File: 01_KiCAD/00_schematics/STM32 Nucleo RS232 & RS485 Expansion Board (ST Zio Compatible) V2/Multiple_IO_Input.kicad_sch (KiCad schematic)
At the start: 0 parts

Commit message: Added components and change device
Added dual Schmidt trigger input SN74LVC2G14DBV for LED Rx and Tx control.
Changed sn74hcs245 for alternate part sn74lvc245a for larger footprint and better availability with LCSC.
Difference is sn74lvc245a has no Schmidt-trigger inputs but instead just normal inputs. Fot details see dataseet. Both devices use exact same pin number and configuration except sn74lvc245a has no thermal pad or exposed pad like the sn74hcs245 has.
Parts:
- added C26: 100nF, PCM_SparkFun-Capacitor:C_0603_1608Metric, symbol PCM_SparkFun-Capacitor:0.1uF_0603_25V_20%
- added D7: LED, IN-S63AT:LED_0603_WRE, symbol PCM_SparkFun-LED:LED
- added J6: HEADER 3POS 2.54mm, symbol Connector_Generic:Conn_01x03
- added Q2: BSS84, Package_TO_SOT_SMD:SOT-23, symbol Transistor_FET:BSS84
- added R23, R24, R37: 100K, PCM_fab:R_0603, symbol PCM_fab:R_0603
- added R32, R33, R36: 10K, PCM_fab:R_0603, symbol PCM_fab:R_0603
- added R34: 1K, PCM_fab:R_0603, symbol PCM_fab:R_0603
- added R35: 590R, PCM_fab:R_0603, symbol PCM_fab:R_0603
- added U3: SN74LVC245ADBR, SN74LVC245ADBR:SOP65P780X200-20N, symbol SN74LVC245ADBR:SN74HCS245RKSR
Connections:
- new net: J6.2 (Pin_2), R37.1, U3.19 (*OE)
- new net: Q2.1 (G), R34.1, R36.1
- new net: D7.2 (A), R35.2
- new net: R24.1, U3.9 (A8)
- new net: R32.2, U3.1 (DIR)
- new net: R23.1, U3.11 (B8)
- new net: J6.1 (Pin_1), R33.2
- new net 3V3_SYS: C26.1, R32.1, R33.1, U3.20 (VCC)
- new net DIR: U3.15 (B4)
- new net GND: C26.2, D7.1 (K), Q2.2 (S), R23.2, R24.2, R36.2, R37.2, U3.10 (GND)
- new net MCU_DIR: U3.5 (A4)
- new net MCU_MODE0: U3.6 (A5)
- new net MCU_MODE1: U3.7 (A6)
- new net MCU_MODE2: U3.8 (A7)
- new net MCU_OE: J6.3 (Pin_3), R35.1
- new net MCU_SLR: U3.2 (A1)
- new net MCU_TERM_RX: U3.4 (A3)
- new net MCU_TERM_TX: U3.3 (A2)
- new net MODE0: U3.14 (B5)
- new net MODE1: U3.13 (B6)
- new net MODE2: U3.12 (B7)
- new net SLR: U3.18 (B1)
- new net TERM_RX: U3.16 (B3)
- new net TERM_TX: U3.17 (B2)

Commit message: Finisching touches to schematics
Finalizing the schematics and double-check all connections throughout the different sheets.
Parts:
- renumbered Q2 to Q1, R34 to R20, R36 to R21, R33 to R22, R32 to R23, R23 to R25, R35 to R26, R37 to R27, U3 to U4
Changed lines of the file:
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@@
 		(dnp no)
 		(fields_autoplaced yes)
-		(property "Reference" "#PWR039"
+		(property "Reference" "#PWR040"
 			(at 144.78 121.92 0)
 			(effects
@@
 			(project "STM32 Nucleo RS232 & RS485 Expansion Board (ST Zio Compatible) V2"
 				(path "/080f83b7-8913-48e8-ab8e-79cb12295542/486090d1-223c-4361-8c2c-169c4ca9272f"
-					(reference "#PWR039")
+					(reference "#PWR040")
 					(unit 1)
 				)
@@
 		(dnp no)
 		(fields_autoplaced yes)
-		(property "Reference" "#PWR038"
+		(property "Reference" "#PWR042"
 			(at 220.98 121.92 0)
 			(effects
@@
 			(project "STM32 Nucleo RS232 & RS485 Expansion Board (ST Zio Compatible) V2"
 				(path "/080f83b7-8913-48e8-ab8e-79cb12295542/486090d1-223c-4361-8c2c-169c4ca9272f"
-					(reference "#PWR038")
+					(reference "#PWR042")
 					(unit 1)
 				)
@@
 		(dnp no)
 		(fields_autoplaced yes)
-		(property "Reference" "R37"
+		(property "Reference" "R27"
 			(at 134.62 105.4099 0)
 			(effects
@@
 			(project "STM32 Nucleo RS232 & RS485 Expansion Board (ST Zio Compatible) V2"
 				(path "/080f83b7-8913-48e8-ab8e-79cb12295542/486090d1-223c-4361-8c2c-169c4ca9272f"
-					(reference "R37")
+					(reference "R27")
 					(unit 1)
 				)
@@
 		(on_board yes)
 		(dnp no)
-		(property "Reference" "Q2"
+		(property "Reference" "Q1"
 			(at -38.1 72.3901 0)
 			(effects
@@
 			(project ""
 				(path "/080f83b7-8913-48e8-ab8e-79cb12295542/486090d1-223c-4361-8c2c-169c4ca9272f"
-					(reference "Q2")
+					(reference "Q1")
 					(unit 1)
 				)
@@
 		(on_board yes)
 		(dnp no)
-		(property "Reference" "R35"
+		(property "Reference" "R26"
 			(at 87.63 105.4099 0)
 			(effects
@@
 			(project "STM32 Nucleo RS232 & RS485 Expansion Board (ST Zio Compatible) V2"
 				(path "/080f83b7-8913-48e8-ab8e-79cb12295542/486090d1-223c-4361-8c2c-169c4ca9272f"
-					(reference "R35")
+					(reference "R26")
 					(unit 1)
 				)
@@
 		(dnp no)
 		(fields_autoplaced yes)
-		(property "Reference" "R32"
+		(property "Reference" "R23"
 			(at 106.68 81.2799 0)
 			(effects
@@
 			(project "STM32 Nucleo RS232 & RS485 Expansion Board (ST Zio Compatible) V2"
 				(path "/080f83b7-8913-48e8-ab8e-79cb12295542/486090d1-223c-4361-8c2c-169c4ca9272f"
-					(reference "R32")
+					(reference "R23")
 					(unit 1)
 				)
@@
 		(dnp no)
 		(fields_autoplaced yes)
-		(property "Reference" "U3"
+		(property "Reference" "U4"
 			(at 185.0233 63.5 0)
 			(effects
@@
 			(project ""
 				(path "/080f83b7-8913-48e8-ab8e-79cb12295542/486090d1-223c-4361-8c2c-169c4ca9272f"
-					(reference "U3")
+					(reference "U4")
 					(unit 1)
 				)
@@
 		(dnp no)
 		(fields_autoplaced yes)
-		(property "Reference" "#PWR040"
+		(property "Reference" "#PWR041"
 			(at 182.88 121.92 0)
 			(effects
@@
 			(project "STM32 Nucleo RS232 & RS485 Expansion Board (ST Zio Compatible) V2"
 				(path "/080f83b7-8913-48e8-ab8e-79cb12295542/486090d1-223c-4361-8c2c-169c4ca9272f"
-					(reference "#PWR040")
+					(reference "#PWR041")
 					(unit 1)
 				)
@@
 		(dnp no)
 		(fields_autoplaced yes)
-		(property "Reference" "#PWR042"
+		(property "Reference" "#PWR037"
 			(at 173.99 63.5 0)
 			(effects
@@
 			(project "STM32 Nucleo RS232 & RS485 Expansion Board (ST Zio Compatible) V2"
 				(path "/080f83b7-8913-48e8-ab8e-79cb12295542/486090d1-223c-4361-8c2c-169c4ca9272f"
-					(reference "#PWR042")
+					(reference "#PWR037")
 					(unit 1)
 				)
@@
 		(on_board yes)
 		(dnp no)
-		(property "Reference" "R23"
+		(property "Reference" "R25"
 			(at 209.55 101.6 90)
 			(effects
@@
 			(project "STM32 Nucleo RS232 & RS485 Expansion Board (ST Zio Compatible) V2"
 				(path "/080f83b7-8913-48e8-ab8e-79cb12295542/486090d1-223c-4361-8c2c-169c4ca9272f"
-					(reference "R23")
+					(reference "R25")
 					(unit 1)
 				)
@@
 		(dnp no)
 		(fields_autoplaced yes)
-		(property "Reference" "R36"
+		(property "Reference" "R21"
 			(at -21.59 77.4699 0)
 			(effects
@@
 			(project "STM32 Nucleo RS232 & RS485 Expansion Board (ST Zio Compatible) V2"
 				(path "/080f83b7-8913-48e8-ab8e-79cb12295542/486090d1-223c-4361-8c2c-169c4ca9272f"
-					(reference "R36")
+					(reference "R21")
 					(unit 1)
 				)
@@
 		(dnp no)
 		(fields_autoplaced yes)
-		(property "Reference" "#PWR044"
+		(property "Reference" "#PWR038"
 			(at -34.29 102.87 0)
 			(effects
@@
 			(project "STM32 Nucleo RS232 & RS485 Expansion Board (ST Zio Compatible) V2"
 				(path "/080f83b7-8913-48e8-ab8e-79cb12295542/486090d1-223c-4361-8c2c-169c4ca9272f"
-					(reference "#PWR044")
+					(reference "#PWR038")
 					(unit 1)
 				)
@@
 		(dnp no)
 		(fields_autoplaced yes)
-		(property "Reference" "R33"
+		(property "Reference" "R22"
 			(at 87.63 81.2799 0)
 			(effects
@@
 			(project "STM32 Nucleo RS232 & RS485 Expansion Board (ST Zio Compatible) V2"
 				(path "/080f83b7-8913-48e8-ab8e-79cb12295542/486090d1-223c-4361-8c2c-169c4ca9272f"
-					(reference "R33")
+					(reference "R22")
 					(unit 1)
 				)
@@
 		(dnp no)
 		(fields_autoplaced yes)
-		(property "Reference" "#PWR047"
+		(property "Reference" "#PWR039"
 			(at 132.08 121.92 0)
 			(effects
@@
 			(project "STM32 Nucleo RS232 & RS485 Expansion Board (ST Zio Compatible) V2"
 				(path "/080f83b7-8913-48e8-ab8e-79cb12295542/486090d1-223c-4361-8c2c-169c4ca9272f"
-					(reference "#PWR047")
+					(reference "#PWR039")
 					(unit 1)
 				)
@@
 		(on_board yes)
 		(dnp no)
-		(property "Reference" "R34"
+		(property "Reference" "R20"
 			(at -18.542 66.04 90)
 			(effects
@@
 			(project "STM32 Nucleo RS232 & RS485 Expansion Board (ST Zio Compatible) V2"
 				(path "/080f83b7-8913-48e8-ab8e-79cb12295542/486090d1-223c-4361-8c2c-169c4ca9272f"
-					(reference "R34")
+					(reference "R20")
 					(unit 1)
 				)

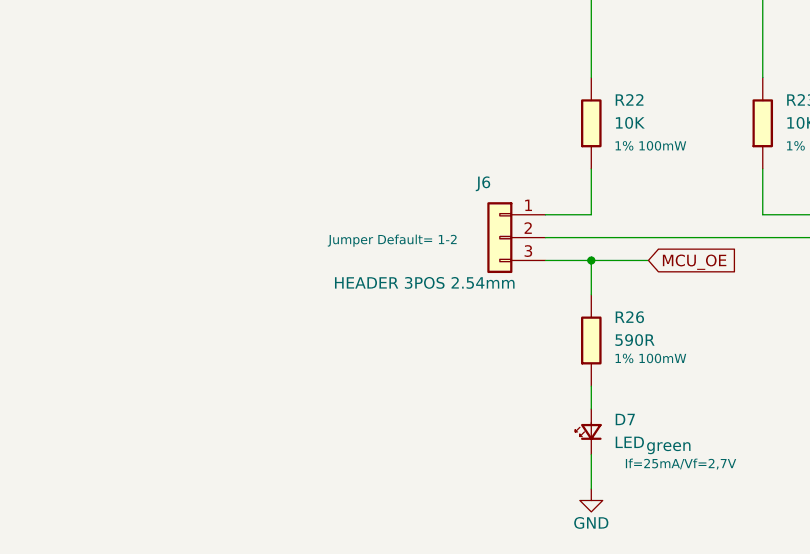
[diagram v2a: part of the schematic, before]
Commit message: Finishing up the schematic aand created the board outline
Made some finishing touches to the schematic, updated all the symbol footprints and started to create the board.
Added missing 3D models for Phoenix 4-p RS485 connector and RS232 connector, also for Inolux LED.
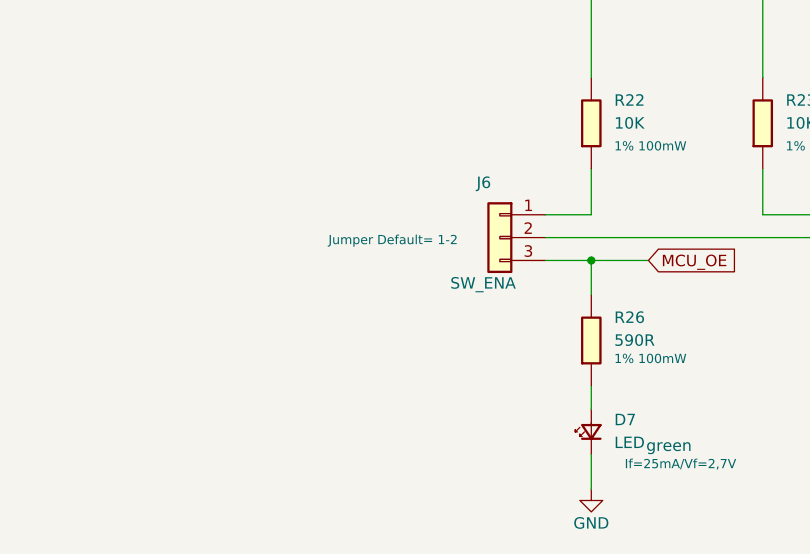
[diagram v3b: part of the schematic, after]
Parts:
- J6: value HEADER 3POS 2.54mm -> SW_ENA; footprint (none) -> HTSW-103-07-F-S:CON3_1X3_TU_TSW
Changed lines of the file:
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@@
 		(dnp no)
 		(fields_autoplaced yes)
-		(property "Reference" "#PWR040"
+		(property "Reference" "#PWR042"
 			(at 144.78 121.92 0)
 			(effects
@@
 			(project "STM32 Nucleo RS232 & RS485 Expansion Board (ST Zio Compatible) V2"
 				(path "/080f83b7-8913-48e8-ab8e-79cb12295542/486090d1-223c-4361-8c2c-169c4ca9272f"
-					(reference "#PWR040")
+					(reference "#PWR042")
 					(unit 1)
 				)
@@
 		(dnp no)
 		(fields_autoplaced yes)
-		(property "Reference" "#PWR043"
+		(property "Reference" "#PWR045"
 			(at 85.09 130.81 0)
 			(effects
@@
 			(project "STM32 Nucleo RS232 & RS485 Expansion Board (ST Zio Compatible) V2"
 				(path "/080f83b7-8913-48e8-ab8e-79cb12295542/486090d1-223c-4361-8c2c-169c4ca9272f"
-					(reference "#PWR043")
+					(reference "#PWR045")
 					(unit 1)
 				)
@@
 		(dnp no)
 		(fields_autoplaced yes)
-		(property "Reference" "#PWR042"
+		(property "Reference" "#PWR044"
 			(at 220.98 121.92 0)
 			(effects
@@
 			(project "STM32 Nucleo RS232 & RS485 Expansion Board (ST Zio Compatible) V2"
 				(path "/080f83b7-8913-48e8-ab8e-79cb12295542/486090d1-223c-4361-8c2c-169c4ca9272f"
-					(reference "#PWR042")
+					(reference "#PWR044")
 					(unit 1)
 				)
@@
 			)
 		)
-		(property "Value" "HEADER 3POS 2.54mm"
+		(property "Value" "SW_ENA"
 			(at 76.708 101.6 0)
 			(effects
@@
 			)
 		)
-		(property "Footprint" ""
+		(property "Footprint" "HTSW-103-07-F-S:CON3_1X3_TU_TSW"
 			(at 74.93 96.52 0)
 			(effects
@@
 			)
 		)
-		(property "Datasheet" "https://www.lcsc.com/datasheet/C6631883.pdf"
+		(property "Datasheet" "~"
 			(at 74.93 96.52 0)
 			(effects
@@
 			)
 		)
-		(property "Description" "Pin Header 3 Position 2.54mm Pitch Single Row Through Hole -55℃~+125℃"
+		(property "Description" "Generic connector, single row, 01x03, script generated (kicad-library-utils/schlib/autogen/connector/)"
 			(at 74.93 96.52 0)
 			(effects
@@
 		(dnp no)
 		(fields_autoplaced yes)
-		(property "Reference" "#PWR041"
+		(property "Reference" "#PWR043"
 			(at 182.88 121.92 0)
 			(effects
@@
 			(project "STM32 Nucleo RS232 & RS485 Expansion Board (ST Zio Compatible) V2"
 				(path "/080f83b7-8913-48e8-ab8e-79cb12295542/486090d1-223c-4361-8c2c-169c4ca9272f"
-					(reference "#PWR041")
+					(reference "#PWR043")
 					(unit 1)
 				)
@@
 		(dnp no)
 		(fields_autoplaced yes)
-		(property "Reference" "#PWR037"
+		(property "Reference" "#PWR039"
 			(at 173.99 63.5 0)
 			(effects
@@
 			(project "STM32 Nucleo RS232 & RS485 Expansion Board (ST Zio Compatible) V2"
 				(path "/080f83b7-8913-48e8-ab8e-79cb12295542/486090d1-223c-4361-8c2c-169c4ca9272f"
-					(reference "#PWR037")
+					(reference "#PWR039")
 					(unit 1)
 				)
@@
 		(dnp no)
 		(fields_autoplaced yes)
-		(property "Reference" "#PWR038"
+		(property "Reference" "#PWR040"
 			(at -34.29 102.87 0)
 			(effects
@@
 			(project "STM32 Nucleo RS232 & RS485 Expansion Board (ST Zio Compatible) V2"
 				(path "/080f83b7-8913-48e8-ab8e-79cb12295542/486090d1-223c-4361-8c2c-169c4ca9272f"
-					(reference "#PWR038")
+					(reference "#PWR040")
 					(unit 1)
 				)
@@
 		(dnp no)
 		(fields_autoplaced yes)
-		(property "Reference" "#PWR039"
+		(property "Reference" "#PWR041"
 			(at 132.08 121.92 0)
 			(effects
@@
 			(project "STM32 Nucleo RS232 & RS485 Expansion Board (ST Zio Compatible) V2"
 				(path "/080f83b7-8913-48e8-ab8e-79cb12295542/486090d1-223c-4361-8c2c-169c4ca9272f"
-					(reference "#PWR039")
+					(reference "#PWR041")
 					(unit 1)
 				)

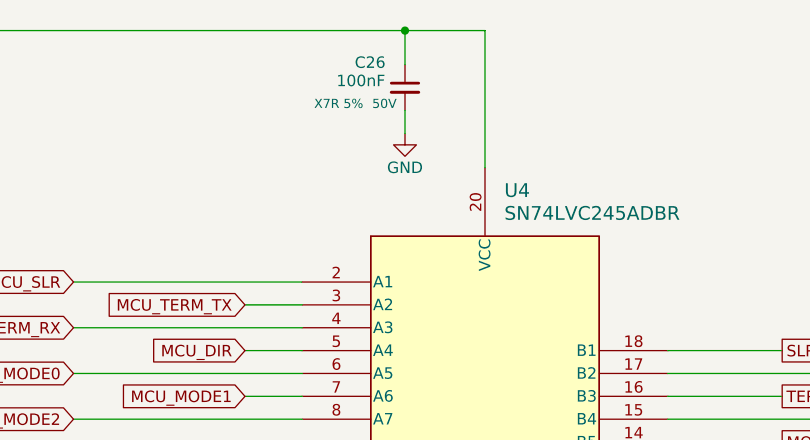
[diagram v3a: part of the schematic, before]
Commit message: Updated footprints and added components to PCB
Added some additional components to the board. Changed the footprint of the 3-pin Jumper so the bottom silkscreen text doesnlt overlap with the Dual Schmidt Trigger IC's SN74LVC2G14
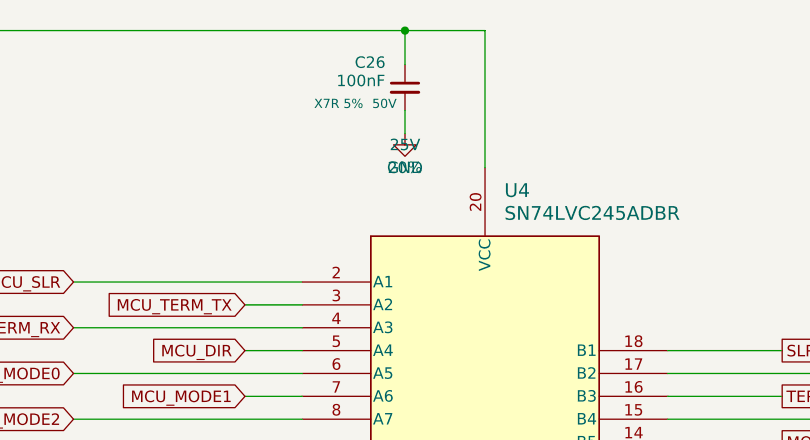
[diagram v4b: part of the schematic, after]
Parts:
- C26: PROD_ID (none) -> CAP-00810; Tolerance (none) -> 20%; Voltage (none) -> 25V
- J6: footprint HTSW-103-07-F-S:CON3_1X3_TU_TSW -> Samtec_Connector:Samtec HTSW-103-07-F-S
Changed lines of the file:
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@@
 			)
 		)
-		(property "Datasheet" "https://www.lcsc.com/datasheet/C14675.pdf"
+		(property "Datasheet" "~"
 			(at 132.08 107.95 0)
 			(effects
@@
 			)
 		)
-		(property "Description" "100mW 100kΩ 75V Thick Film Resistor ±100ppm/℃ ±1% 0603 Chip Resistor - Surface Mount RoHS"
+		(property "Description" "Resistor"
 			(at 132.08 107.95 0)
 			(effects
@@
 			)
 		)
-		(property "Datasheet" "https://www.lcsc.com/datasheet/C91183.pdf"
+		(property "Datasheet" "https://cdn.sparkfun.com/assets/8/a/4/a/5/Kemet_Capacitor_Datasheet.pdf"
 			(at 173.99 66.04 0)
 			(effects
@@
 			)
 		)
-		(property "Description" "100nF ±5% 50V Ceramic Capacitor X7R 0603"
+		(property "Description" "Unpolarized capacitor"
 			(at 173.99 71.12 0)
 			(effects
@@
 					(size 1.016 1.016)
 					(color 194 0 0 1)
+				)
+			)
+		)
+		(property "PROD_ID" "CAP-00810"
+			(at 173.99 68.58 0)
+			(effects
+				(font
+					(size 1.27 1.27)
+				)
+				(hide yes)
+			)
+		)
+		(property "Voltage" "25V"
+			(at 173.99 58.42 0)
+			(effects
+				(font
+					(size 1.27 1.27)
+				)
+			)
+		)
+		(property "Tolerance" "20%"
+			(at 173.99 60.96 0)
+			(effects
+				(font
+					(size 1.27 1.27)
 				)
 			)
@@
 			)
 		)
-		(property "Datasheet" "https://www.lcsc.com/datasheet/C22548.pdf"
+		(property "Datasheet" "~"
 			(at 85.09 107.95 0)
 			(effects
@@
 			)
 		)
-		(property "Description" "100mW 1kΩ 75V Thick Film Resistor ±100ppm/℃ ±1% 0603 Chip Resistor - Surface Mount RoHS"
+		(property "Description" "Resistor"
 			(at 85.09 107.95 0)
 			(effects
@@
 			)
 		)
-		(property "Datasheet" "https://www.lcsc.com/datasheet/C14675.pdf"
+		(property "Datasheet" "~"
 			(at 156.21 99.06 0)
 			(effects
@@
 			)
 		)
-		(property "Description" "100mW 100kΩ 75V Thick Film Resistor ±100ppm/℃ ±1% 0603 Chip Resistor - Surface Mount RoHS"
+		(property "Description" "Resistor"
 			(at 156.21 99.06 0)
 			(effects
@@
 			)
 		)
-		(property "Datasheet" "https://www.lcsc.com/datasheet/C98220.pdf"
+		(property "Datasheet" "~"
 			(at 104.14 83.82 0)
 			(effects
@@
 			)
 		)
-		(property "Description" "100mW 10kΩ 75V Thick Film Resistor ±100ppm/℃ ±1% 0603 Chip Resistor - Surface Mount RoHS"
+		(property "Description" "Resistor"
 			(at 104.14 83.82 0)
 			(effects
@@
 			)
 		)
-		(property "Footprint" "HTSW-103-07-F-S:CON3_1X3_TU_TSW"
+		(property "Footprint" "Samtec_Connector:Samtec HTSW-103-07-F-S"
 			(at 74.93 96.52 0)
 			(effects
@@
 			)
 		)
-		(property "Datasheet" "https://www.lcsc.com/datasheet/C14675.pdf"
+		(property "Datasheet" "~"
 			(at 209.55 99.06 0)
 			(effects
@@
 			)
 		)
-		(property "Description" "100mW 100kΩ 75V Thick Film Resistor ±100ppm/℃ ±1% 0603 Chip Resistor - Surface Mount RoHS"
+		(property "Description" "Resistor"
 			(at 209.55 99.06 0)
 			(effects
@@
 			)
 		)
-		(property "Datasheet" "https://www.lcsc.com/datasheet/C98220.pdf"
+		(property "Datasheet" "~"
 			(at -24.13 80.01 0)
 			(effects
@@
 			)
 		)
-		(property "Description" "100mW 10kΩ 75V Thick Film Resistor ±100ppm/℃ ±1% 0603 Chip Resistor - Surface Mount RoHS"
+		(property "Description" "Resistor"
 			(at -24.13 80.01 0)
 			(effects
@@
 			)
 		)
-		(property "Datasheet" "https://www.lcsc.com/datasheet/C5656662.pdf"
+		(property "Datasheet" "~"
 			(at 92.71 118.11 0)
 			(effects
@@
 			)
 		)
-		(property "Description" "Emerald Green 530nm LED Indication - Discrete 2.7V 0603"
+		(property "Description" "Light emitting diode"
 			(at 97.79 118.11 0)
 			(effects
@@
 			)
 		)
-		(property "Datasheet" "https://www.lcsc.com/datasheet/C98220.pdf"
+		(property "Datasheet" "~"
 			(at 85.09 83.82 0)
 			(effects
@@
 			)
 		)
-		(property "Description" "100mW 10kΩ 75V Thick Film Resistor ±100ppm/℃ ±1% 0603 Chip Resistor - Surface Mount RoHS"
+		(property "Description" "Resistor"
 			(at 85.09 83.82 0)
 			(effects
@@
 			)
 		)
-		(property "Datasheet" "https://www.lcsc.com/datasheet/C22548.pdf"
+		(property "Datasheet" "~"
 			(at -15.24 71.12 0)
 			(effects
@@
 			)
 		)
-		(property "Description" "100mW 1kΩ 75V Thick Film Resistor ±100ppm/℃ ±1% 0603 Chip Resistor - Surface Mount RoHS"
+		(property "Description" "Resistor"
 			(at -15.24 71.12 0)
 			(effects

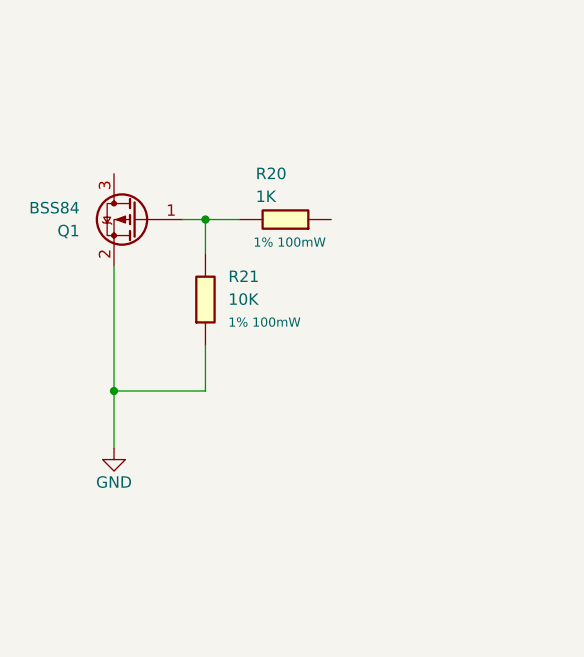
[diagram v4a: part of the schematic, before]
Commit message: Added half-duplex jumpers
Addres jumpers for hardware RS485 half-duplex configuration combining signals A(Y) & B(Z). Finalising testpoints and added 3D models for each test-point color.
-Green = logic side
-Blue = connector side
Made some minor changed to layout for test signals clarification (THVD4431 sheet)
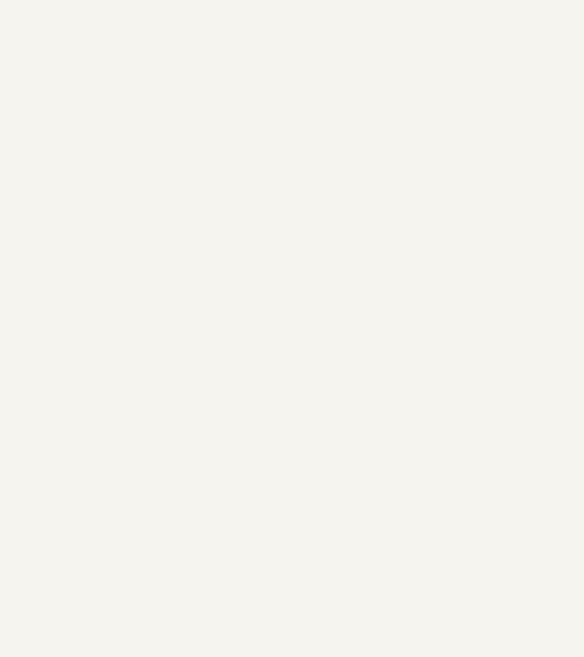
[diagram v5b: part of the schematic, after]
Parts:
- removed Q1: BSS84, Package_TO_SOT_SMD:SOT-23, symbol Transistor_FET:BSS84
- removed R20: 1K, PCM_fab:R_0603, symbol PCM_fab:R_0603
- removed R21: 10K, PCM_fab:R_0603, symbol PCM_fab:R_0603
